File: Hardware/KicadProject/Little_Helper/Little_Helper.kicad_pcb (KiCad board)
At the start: 4 copper layers, 84 x 25.6 mm, 38 parts, among them J1 USB_B_Micro_Molex_1050171001_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, J2 SOLDER_CON_5x2_TOP, J3 SOLDER_CON_5x2_TOP, Q1 DMG3415U, SW1 SW_Push, SW2 SW_Push, SW3 SW_Push, SW4 SW_Push, SW5 SW_Push, SW6 SW_On_On, SW7 SW_Tactile_Small, SW8 SW_Tactile_Small, U1 AP2112K-3.3, U2 ESP32-S3-MINI-1, U3 MCP73831-2-OT

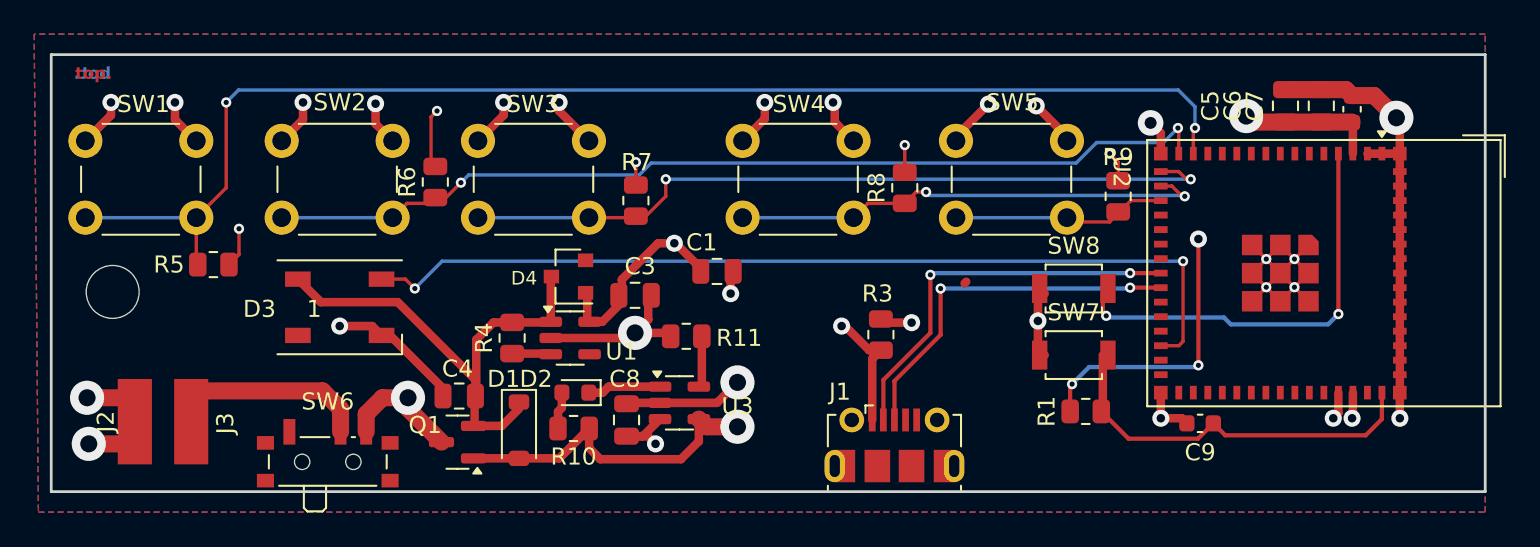
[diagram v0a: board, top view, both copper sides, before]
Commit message: switch to board V1.1 version
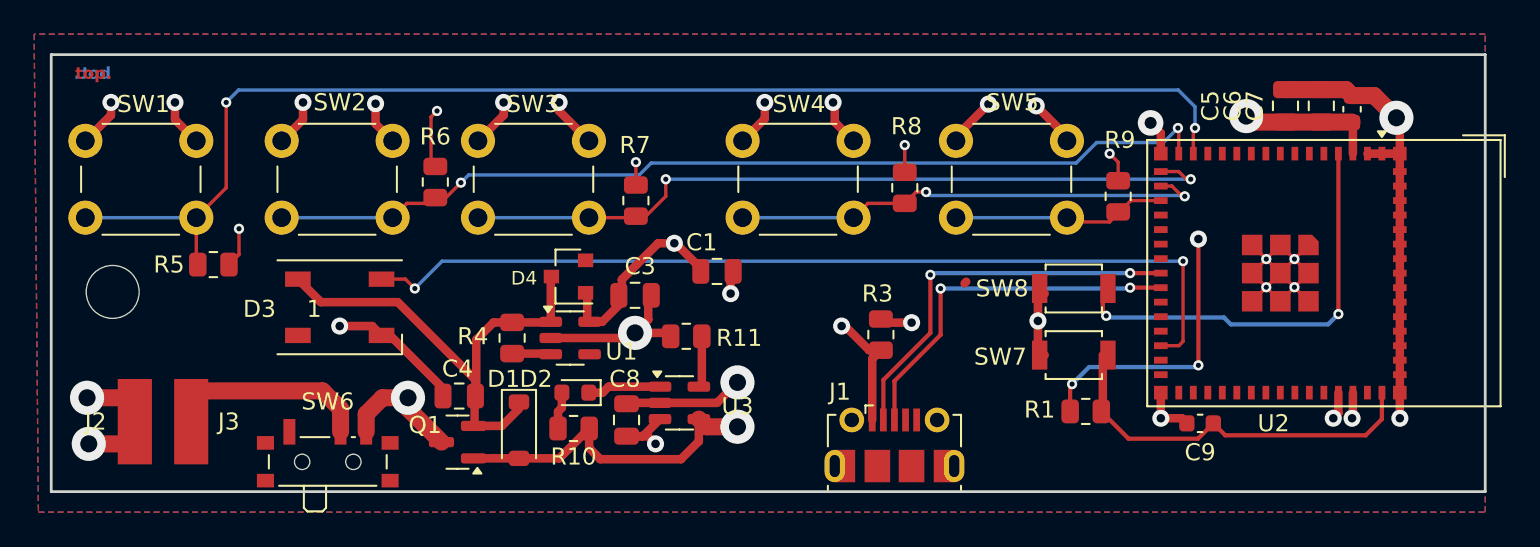
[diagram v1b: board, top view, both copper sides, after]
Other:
- board text added: "WOLKE Little Helper V1.1"
- board text removed: "WOLKE Little Helper V1.0"
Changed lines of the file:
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@@
 		(tags "2.4 GHz Wi-Fi Bluetooth external antenna espressif  20*15.4mm")
 		(property "Reference" "U2"
-			(at -5.95 11.85 -90)
+			(at 8.8 2.95 0)
 			(unlocked yes)
 			(layer "F.SilkS")
@@
 		(tags "resistor")
 		(property "Reference" "R1"
-			(at -2.2875 0 90)
+			(at -2.7 -0.1 180)
 			(layer "F.SilkS")
 			(effects
@@
 		(tags "Tactile Switch")
 		(property "Reference" "SW8"
-			(at 0 -2.5 0)
+			(at -4.2 0 0)
 			(layer "F.SilkS")
 			(effects
@@
 		)
 		(fp_text user "${REFERENCE}"
-			(at 0 -2.5 0)
+			(at -4.2 0 0)
 			(layer "F.Fab")
 			(effects
@@
 		(tags "Tactile Switch")
 		(property "Reference" "SW7"
-			(at 0 -2.5 0)
+			(at -4.3 0.1 0)
 			(layer "F.SilkS")
 			(effects
@@
 		)
 		(fp_text user "${REFERENCE}"
-			(at 0 -2.5 0)
+			(at -4.3 0.1 0)
 			(layer "F.Fab")
 			(effects
@@
 		(tags "resistor")
 		(property "Reference" "R6"
-			(at 0 -1.65 -90)
+			(at 2.6625 0 0)
 			(layer "F.SilkS")
 			(effects
@@
 		(tags "resistor")
 		(property "Reference" "R7"
-			(at 2.25 0.05 0)
+			(at 3.25 -0.05 0)
 			(layer "F.SilkS")
 			(effects
@@
 		(at -33.8 8.7 90)
 		(property "Reference" "J3"
-			(at -0.1 2 90)
+			(at 0 2.2 180)
 			(layer "F.SilkS")
 			(effects
@@
 		(at -37.1 8.7 90)
 		(property "Reference" "J2"
-			(at 0 -1.7 90)
+			(at 0 -2.3 180)
 			(layer "F.SilkS")
 			(effects
@@
 		(tags "resistor")
 		(property "Reference" "R8"
-			(at 0 -1.65 -90)
+			(at 3.6 0.1 0)
 			(layer "F.SilkS")
 			(effects
@@
 		(tags "resistor")
 		(property "Reference" "R4"
-			(at 0 -1.65 -90)
+			(at 0.1 -2.3 0)
 			(layer "F.SilkS")
 			(effects
@@
 		(tags "resistor")
 		(property "Reference" "R9"
-			(at 2.3 0 0)
+			(at 3.3 0.1 0)
 			(layer "F.SilkS")
 			(effects
@@
 		)
 	)
-	(gr_text "WOLKE\nLittle Helper V1.0"
+	(gr_text "WOLKE\nLittle Helper V1.1"
 		(at 34.3 6.6 270)
 		(layer "B.Mask")

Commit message: edit pcb and footprints for pcb rev1.1
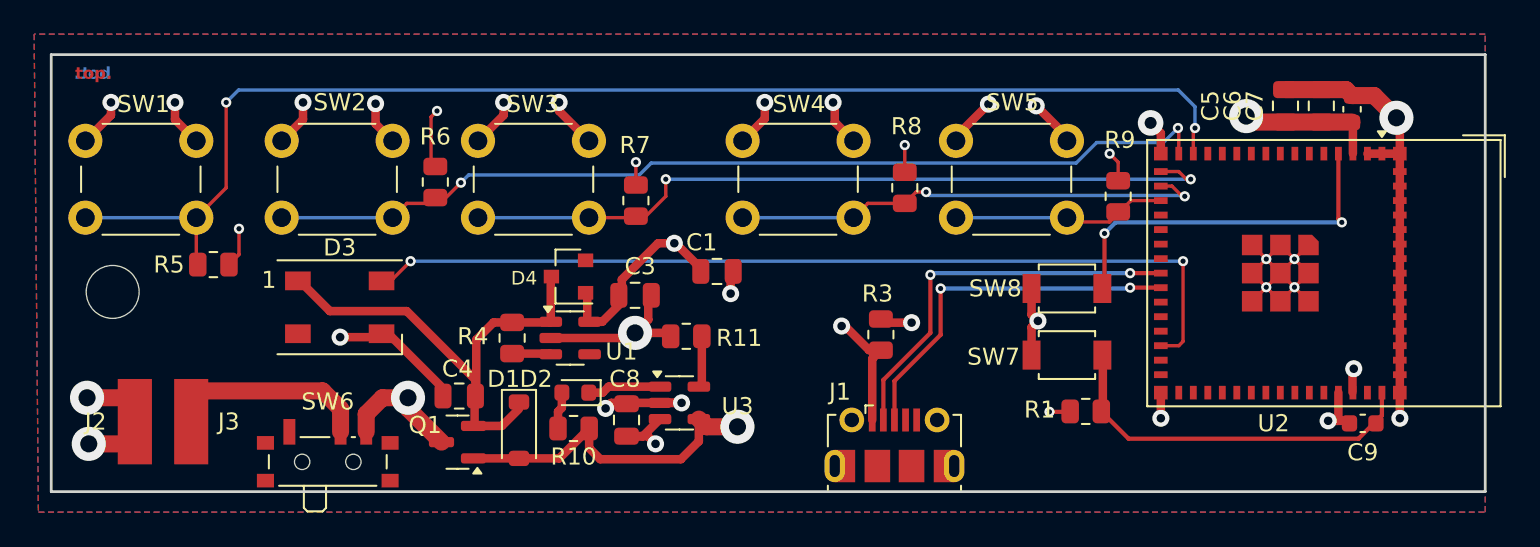
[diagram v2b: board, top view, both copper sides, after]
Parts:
- D3: footprint LED_SMD:LED_WS2812B_PLCC4_5.0x5.0mm_P3.2mm -> led_smd_JLCPCB:LED_WS2812B_JLCPCB_5.0x5.0mm_P3.2mm
- moved C9 9.53 mm to (34.8, 8.80)
- moved SW7 0.40 mm to (17.5, 4.80)
- moved SW8 0.40 mm to (17.5, 0.90)
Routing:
- net +3.3V: track 48.1 -> 32.4 mm, vias 10 -> 8
- net /BOOT0: track 24.8 -> 21.8 mm
- net /RESET: track 23.0 -> 22.3 mm
- net GND: track 121.8 -> 121.2 mm, vias 28 -> 29

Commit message: pcb v1.1 add second ws2812 led
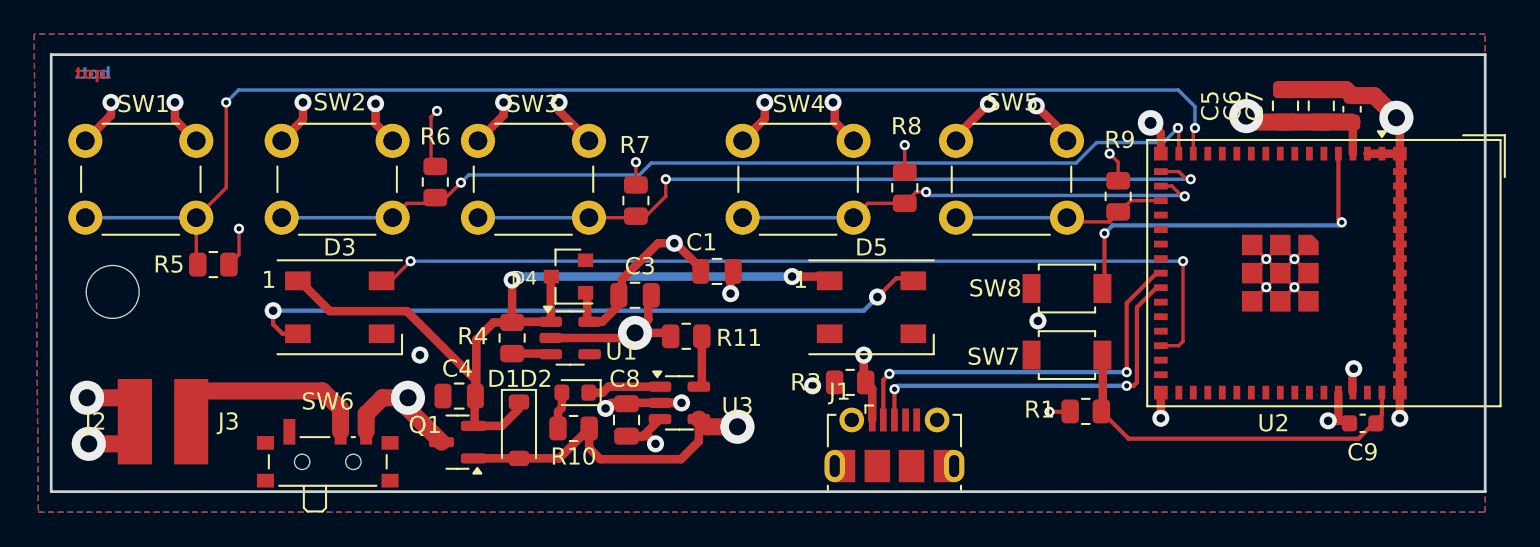
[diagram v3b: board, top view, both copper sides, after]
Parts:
- added D5: WS2812B, led_smd_JLCPCB:LED_WS2812B_JLCPCB_5.0x5.0mm_P3.2mm, F.Cu at (6.05, 2.00)
- moved R3 3.33 mm to (4.80, 6.40), turned to 0 degrees
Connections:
- net /BOOT0 renamed Net-(U2-IO0)
- net /RESET renamed Net-(U2-EN)
- D3 pad 2: unconnected-(D3-DOUT-Pad2) -> Net-(D3-DOUT)
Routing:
- net Net-(D3-DOUT): track 0.00 -> 40.8 mm, vias 0 -> 2
- net /NEOPIX_VDD: track 29.5 -> 50.9 mm, vias 0 -> 2
- net GND: track 121.2 -> 108.1 mm
- net VBUS: track 26.7 -> 23.5 mm
- net /Usb_D+: track 21.7 -> 22.4 mm

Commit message: add batterie voltage divider. add colorchooser. this commit produce an major bug in button mapping. 2. Map is completly broken.
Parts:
- added R12: 47K, ba_res:r2012, F.Cu at (12.1, 1.70)
- added R13: 18K, ba_res:r2012, F.Cu at (12.1, 3.90)
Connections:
- U2 pad 10: unconnected-(U2-IO6-Pad10) -> /BattVoltDiv
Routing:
- net /BattVoltDiv: track 0.00 -> 24.9 mm, vias 0 -> 2
- net /NEOPIX_VDD: track 50.9 -> 63.4 mm

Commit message: add firmware v7 bin file
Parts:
- moved C4 11.1 mm to (-29.2, 6.88)
- moved Q1 0.15 mm to (-18.1, 9.78)
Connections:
- C4 pad 1: /NEOPIX_VDD -> Net-(D1-K)
- D1 pad 1: /NEOPIX_VDD -> Net-(D1-K)
- J3 pad 1: Net-(J3-P1) -> +BATT
- Q1 pad 2: /NEOPIX_VDD -> Net-(D1-K)
- SW6 pad 2: Net-(J3-P1) -> Net-(D1-K)
- SW6 pad 3: +BATT -> /NEOPIX_VDD
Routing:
- net Net-(D1-K): track 0.00 -> 19.4 mm, vias 0 -> 2
- net +BATT: track 11.4 -> 25.3 mm, vias 2 -> 3
- net Net-(J3-P1): track 11.0 -> 0.00 mm
- net /NEOPIX_VDD: track 63.4 -> 59.8 mm
